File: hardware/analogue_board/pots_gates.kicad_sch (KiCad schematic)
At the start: 57 parts, among them J601 Pot wiper holes; POT_TOP = +3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, J602 Gate out holes, J603 Gate expansion: QH', SRCLK, R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, U601 MCP3208-CI/SL, U602 74HCT595D

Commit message: Analogue board: block review applied, TRS MIDI, ESP32-P4 support
Checkpoint 1 schematic rebuilt after a block-by-block prior-art review
(docs/analogue_board_review/, seven reports and an index).

Schematic:
- Codec: 20 Vpp in and out (15k input feedback; balanced MFB output,
  gain 2.5, 1 nF C0G); ferrite and 5.1 ohm on the codec supplies; VCOM
  decoupled at each input; CODEC_RST to a hole.
- Power: 680 ohm minimum load on +3V3D; buck input ferrite and EN
  divider; SS34 at D201-D203; Q201/JP201 MOD_5V bypass for the ESP32-P4.
- CV in: 15 V TVS at each jack, 1 nF at each ADC input, 1206 outputs.
- CV out: 12k/22k offset with 1 nF, 33k gain; CV7-8 feedback from the
  jack side of the 1k.
- Gates and panel: CS_595 pull-up, GATE_OE_N on J603, 1M wiper
  pull-downs, POT_REF, button RC order, 47 uF at the LED holes.
- New sheet 10: TRS MIDI (Type A), H11L1 in, 5 V buffered out.
- Layout: no overlapping text on any sheet.

ERC 0/0; netlist identical to intent (345 nets); 21 ICs against
datasheets; 17 Extended part types.

Spec v0.4: David's decisions (TVS yes, CV +/-5 V with a +/-10 V
variant, ESP32-P4 accommodated, power header free to move), the
corrections, and a firmware requirements list in section 15.

Co-Authored-By: Claude Opus 5.5 <noreply@anthropic.com>
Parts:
- removed J603: Gate expansion: QH', SRCLK, RCLK, Connector_PinHeader_2.54mm:PinHeader_1x05_P2.54mm_Vertical, symbol Connector_Generic:Conn_01x05
- added J603: Gate expansion: QH', SRCLK, RCLK, OE, Connector_PinHeader_2.54mm:PinHeader_1x06_P2.54mm_Vertical, symbol Connector_Generic:Conn_01x06
- added R627, R628: 1k, Resistor_SMD:R_0402_1005Metric, symbol Device:R_Small
- C603: value 1u 25V -> 10u 25V; footprint Capacitor_SMD:C_0402_1005Metric -> Capacitor_SMD:C_0805_2012Metric; Decouples U601 VREF pin 15 -> U601 VREF pin 15 (POT_REF); LCSC C52923 -> C15850
- C604: Decouples U601 VREF pin 15 -> U601 VREF pin 15 (POT_REF)
- J601: value Pot wiper holes; POT_TOP = +3V3A -> Pot wiper holes; pot tops to POT_REF
- R601: value 10k -> 100R; footprint Resistor_SMD:R_0402_1005Metric -> Resistor_SMD:R_0805_2012Metric; LCSC C25744 -> C17408; Note keeps the pot ADC deselected while the module boots -> isolates the pot reference from the DAC supply
- R602: value 1k -> 10k; LCSC C11702 -> C25744; Note (none) -> keeps the pot ADC deselected while the module boots
- R603, R605, R607, R609, R611, R613, R615, R617: value 100k -> 1k; LCSC C25741 -> C11702
- R604, R606, R608, R610, R612, R614, R616: value 1k -> 1M; LCSC C11702 -> C26083
- R618: value 10k -> 1M; LCSC C25744 -> C26083; Note OE pull-up: gates off until firmware enables -> (none)
- R619: value 1k -> 10k; LCSC C11702 -> C25744; Note (none) -> OE pull-up: gates off until firmware enables
- R620: value 1k -> 10k; LCSC C11702 -> C25744; Note (none) -> latch held idle while the module boots or reflashes
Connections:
- net +3V3A: now also R601.1; no longer C603.1, C604.1, J601.10 (Pin_10), J601.9 (Pin_9), U601.15 (Vref)
- net +3V3D: now also R602.1, R619.1, R620.1; no longer R601.1, R618.1
- net +5VD: now also J603.5 (Pin_5)
- net CS_595: now also R620.2, J603.3 (Pin_3)
- net CS_POT: now also R602.2; no longer R601.2
- net GATE_OE_N: now also R619.2, J603.4 (Pin_4); no longer R618.2
- net GATE_SER_OUT: now also J603.1 (Pin_1)
- net GND: now also R604.2, R606.2, R608.2, R610.2, R612.2, R614.2, R616.2, R618.2, J603.6 (Pin_6); no longer R603.2, R605.2, R607.2, R609.2, R611.2, R613.2, R615.2, R617.2
- net GOUT1: now also R621.2; no longer R619.2
- net GOUT2: now also R622.2; no longer R620.2
- net GOUT3: now also R623.2; no longer R621.2
- net GOUT4: now also R624.2; no longer R622.2
- net GOUT5: now also R625.2; no longer R623.2
- net GOUT6: now also R626.2; no longer R624.2
- net GOUT7: now also R627.2; no longer R625.2
- net GOUT8: now also R628.2; no longer R626.2
- net GQ1: now also R621.1; no longer R619.1
- net GQ2: now also R622.1; no longer R620.1
- net GQ3: now also R623.1; no longer R621.1
- net GQ4: now also R624.1; no longer R622.1
- net GQ5: now also R625.1; no longer R623.1
- net GQ6: now also R626.1; no longer R624.1
- net GQ7: now also R627.1; no longer R625.1
- net GQ8: now also R628.1; no longer R626.1
- net POT1: now also R603.1; no longer R602.1
- net POT2: now also R605.1; no longer R604.1
- net POT3: now also R607.1; no longer R606.1
- net POT4: now also R609.1; no longer R608.1
- net POT5: now also R611.1; no longer R610.1
- net POT6: now also R613.1; no longer R612.1
- net POT7: now also R615.1; no longer R614.1
- net POT8: now also R617.1; no longer R616.1
- net POT_IN1: now also R603.2, R604.1; no longer R602.2, R603.1
- net POT_IN2: now also R605.2, R606.1; no longer R604.2, R605.1
- net POT_IN3: now also R607.2, R608.1; no longer R606.2, R607.1
- net POT_IN4: now also R609.2, R610.1; no longer R608.2, R609.1
- net POT_IN5: now also R611.2, R612.1; no longer R610.2, R611.1
- net POT_IN6: now also R613.2, R614.1; no longer R612.2, R613.1
- net POT_IN7: now also R615.2, R616.1; no longer R614.2, R615.1
- net POT_IN8: now also R617.2, R618.1; no longer R616.2, R617.1
- net SPIB_SCK: now also J603.2 (Pin_2)
- new net POT_REF: C603.1, C604.1, J601.10 (Pin_10), J601.9 (Pin_9), R601.2, U601.15 (Vref)
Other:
- note added: "Chain a second 74HCT595 off-board from J603 (74HCT595 only: a 74HC595 at 5 V needs 3.15 V inputs). OE keeps it off at boot too."
- note added: "Pot tops to the POT_REF holes, bottoms to GND (the deck's D bus)."
- note added: "Pots: MCP3208 on +3V3A. Its VREF and the pot tops share POT_REF (100 Ω + 10 µF from +3V3A), so readings are ratiometric and the hand-wired pot leads can't disturb the DAC's supply. Each wiper: 1 kΩ + 100 nF, 1 MΩ to ground so an unwired channel reads 0 (100 kΩ would bend a 100 kΩ pot's response by up to 12 %). Gate outs: 74HCT595 at 5 V (VIH 2.0 V, so 3.3 V logic drives it) → 1 kΩ → jack, BAV99 c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"
- note added: "SRCLR tied high. Boot order: OE off, clear the register, then enable (firmware)."
- note removed: "Chain a second 74HCT595 off-board from J603 (Boy's expander needs more gate outs)."
- note removed: "Pot tops to the +3V3A holes, bottoms to GND (the deck's D bus)."
- note removed: "Pots: MCP3208 on +3V3A with VREF = +3V3A, and the pot tops fed from the same rail (POT_TOP holes), so readings are ratiometric. Each wiper: 1 kΩ + 100 nF, 100 kΩ to ground so an unwired channel reads 0. Gate outs: 74HCT595 at 5 V (VIH 2.0 V, so 3.3 V logic drives it) → 1 kΩ → jack, BAV99 clamps to +5VD and GND. OE is held high (outputs off) by a pull-up until firmware drives GATE_OE_N low: the 59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"
- note removed: "SRCLR tied high"
- moved on the sheet: C604

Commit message: Analogue board: checkpoint 3 started; double-sided, floorplan placed
- pcb.py generates analogue_board.kicad_pcb from the netlist: outline,
  JLC 4-layer stack-up, every footprint with nets and schematic links
  (KiCad schematic parity: 0 differences), parked parts beside the board,
  courtyard area budget, DRC and 3D renders of both faces.
- Area budget: the courtyards need 104% of one face before routing, so
  David chose double-sided assembly (JLC Standard PCBA, about $100 more
  per order, to confirm on a quote).
- Floorplan in placement.py: analogue ICs at the top under the modules,
  furthest from the buck; logic below; power bottom right around J201;
  MIDI bottom left; 99 wiring-field holes in three columns lined up with
  the edge-strip positions, each group beside its circuit.
- Library: module socket courtyards cover only their header rows; the
  wiring holes get their own footprint with a one-pitch courtyard.
- Spec records the decision, the floorplan and David's answers: 11 mm to
  the deck in 10HP (deck parts 2 mm at most); holes tinned both faces.

Co-Authored-By: Claude Opus 5.5 <noreply@anthropic.com>
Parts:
- J601: footprint Connector_PinHeader_2.54mm:PinHeader_1x12_P2.54mm_Vertical -> analogue_board:WiringHoles_1x12
- J602: footprint Connector_PinHeader_2.54mm:PinHeader_1x10_P2.54mm_Vertical -> analogue_board:WiringHoles_1x10
- J603: footprint Connector_PinHeader_2.54mm:PinHeader_1x06_P2.54mm_Vertical -> analogue_board:WiringHoles_1x06
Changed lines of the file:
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@@
 			)
 		)
-		(property "Footprint" "Connector_PinHeader_2.54mm:PinHeader_1x12_P2.54mm_Vertical"
+		(property "Footprint" "analogue_board:WiringHoles_1x12"
 			(at 185.42 76.2 0)
 			(effects
@@
 			)
 		)
-		(property "Footprint" "Connector_PinHeader_2.54mm:PinHeader_1x10_P2.54mm_Vertical"
+		(property "Footprint" "analogue_board:WiringHoles_1x10"
 			(at 370.84 76.2 0)
 			(effects
@@
 			)
 		)
-		(property "Footprint" "Connector_PinHeader_2.54mm:PinHeader_1x06_P2.54mm_Vertical"
+		(property "Footprint" "analogue_board:WiringHoles_1x06"
 			(at 370.84 160.02 0)
 			(effects

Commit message: Analogue board: first-pass placement; space reclaimed; four wiring banks
- autoplace.py places every unanchored part as close as it fits to the
  pins it connects to: decoupling capacitors at their pin, chains growing
  from their ICs, the buck's loop kept on one face. All 430 parts placed;
  DRC courtyards clean, schematic parity clean, heights checked (<= 2.5 mm
  under the modules, <= 8 mm in the USB keep-outs).
- Space reclaimed (David): Teensy socket without holes for its unused
  far-end pins 20-28 (headers 1x19 + 1x20); right strip (10HP only) without
  holes at 11-15 and 26-30, and outer hole only at 10, 16, 31. checks.py
  lets a project footprint omit only pins the netlist leaves unconnected.
- 74HCT595 in TSSOP-16 (74HCT595PW, C99710, same pinout) sideways in the
  right channel; vertical Qwiic socket (BM04B-SRSS-TB, C160390) below the
  modules, its cable straight up (the side-entry plug had no clear run).
- Wiring field as four mixed banks (David): each quarter of the board has
  some of every channel type, 50/50 left and right, jack-detect holes
  beside their inputs; wiring.py holds the plan, schematic and placement
  both read it. 94 holes.
- Reference designators off the silkscreen for passives and hole groups.

Co-Authored-By: Claude Opus 5.5 <noreply@anthropic.com>
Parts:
- removed J602: Gate out holes, analogue_board:WiringHoles_1x10, symbol Connector_Generic:Conn_01x10
- added J611, J613: Holes, left bottom, analogue_board:WiringHoles_1x03, symbol Connector_Generic:Conn_01x03
- added J612: Holes, left top, analogue_board:WiringHoles_1x03, symbol Connector_Generic:Conn_01x03
- added J614: Holes, right top, analogue_board:WiringHoles_1x05, symbol Connector_Generic:Conn_01x05
- added J615: Holes, right middle, analogue_board:WiringHoles_1x05, symbol Connector_Generic:Conn_01x05
- J610: renamed from J601; value Pot wiper holes; pot tops to POT_REF -> Holes, left top; footprint analogue_board:WiringHoles_1x12 -> analogue_board:WiringHoles_1x03; symbol Connector_Generic:Conn_01x12 -> Connector_Generic:Conn_01x03
- U602: value 74HCT595D -> 74HCT595PW; footprint Package_SO:SOIC-16_3.9x9.9mm_P1.27mm -> Package_SO:TSSOP-16_4.4x5mm_P0.65mm; LCSC C282339 -> C99710; MPN 74HCT595D,118 -> 74HCT595PW,118
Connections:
- net GND: now also J612.2 (Pin_2), J613.2 (Pin_2); no longer J610.11 (Pin_11), J610.12 (Pin_12)
- net GOUT1: now also J610.3 (Pin_3)
- net GOUT2: now also J612.3 (Pin_3)
- net GOUT3: now also J611.3 (Pin_3)
- net GOUT4: now also J613.3 (Pin_3)
- net GOUT5: now also J614.4 (Pin_4)
- net GOUT6: now also J614.5 (Pin_5)
- net GOUT7: now also J615.4 (Pin_4)
- net GOUT8: now also J615.5 (Pin_5)
- net POT2: now also J612.1 (Pin_1); no longer J610.2 (Pin_2)
- net POT3: now also J611.1 (Pin_1); no longer J610.3 (Pin_3)
- net POT4: now also J613.1 (Pin_1); no longer J610.4 (Pin_4)
- net POT5: now also J614.1 (Pin_1); no longer J610.5 (Pin_5)
- net POT6: now also J614.2 (Pin_2); no longer J610.6 (Pin_6)
- net POT7: now also J615.1 (Pin_1); no longer J610.7 (Pin_7)
- net POT8: now also J615.2 (Pin_2); no longer J610.8 (Pin_8)
- net POT_REF: now also J610.2 (Pin_2), J611.2 (Pin_2), J614.3 (Pin_3), J615.3 (Pin_3); no longer J610.10 (Pin_10), J610.9 (Pin_9)
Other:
- note removed: "Pot tops to the POT_REF holes, bottoms to GND (the deck's D bus)."

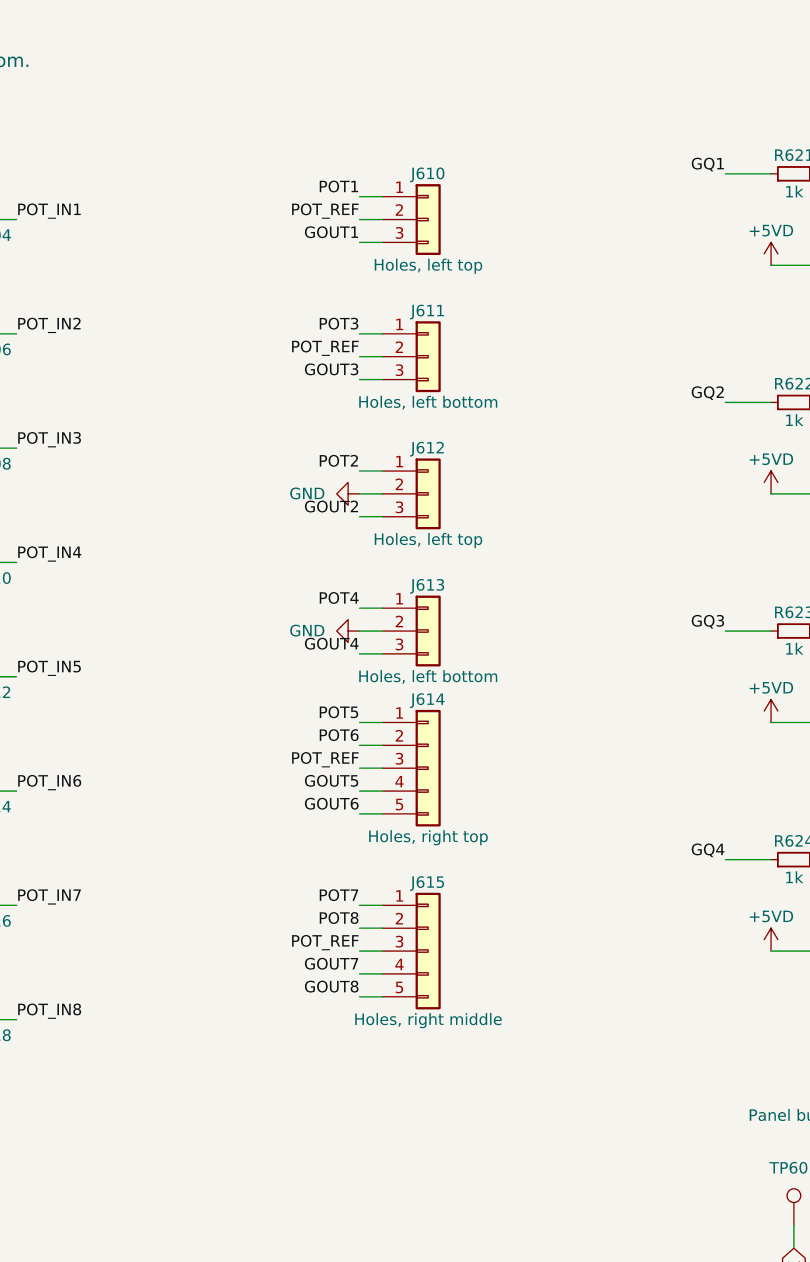
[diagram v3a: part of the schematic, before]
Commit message: Analogue board: bus chips level with their module pins; design rules; trial autoroute
Re-floorplan the centre channel in the order of the module's buses (SPI-A,
SPI-B, I2S, I2C), so the codec is 6 mm from the Pico's I2S pins instead of
38 mm; CV output op-amps move to the top-right corner.

Net classes (0.15/0.15 default, 0.3 power) and an In1 ground plane are
written into the project. autoroute.py runs Freerouting on a copy of the
board to measure routability. Schematic hole groups no longer overlap.

Co-Authored-By: Claude Opus 5.5 <noreply@anthropic.com>
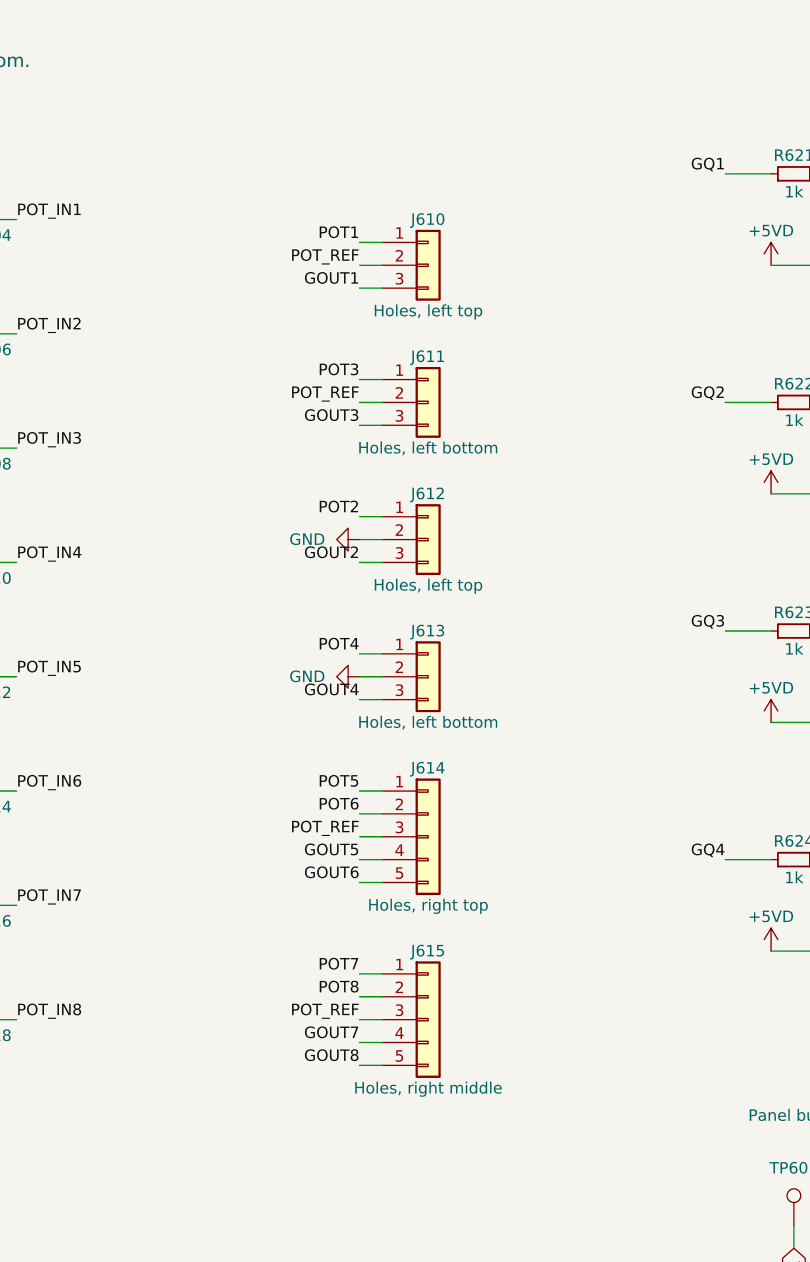
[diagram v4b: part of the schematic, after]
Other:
- moved on the sheet: J610, J611, J612, J613, J614, J615
